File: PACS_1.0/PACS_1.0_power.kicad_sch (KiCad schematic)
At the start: 16 parts, among them U2 TPS562201DDCR, U6 S-1011A70-M6T1U4

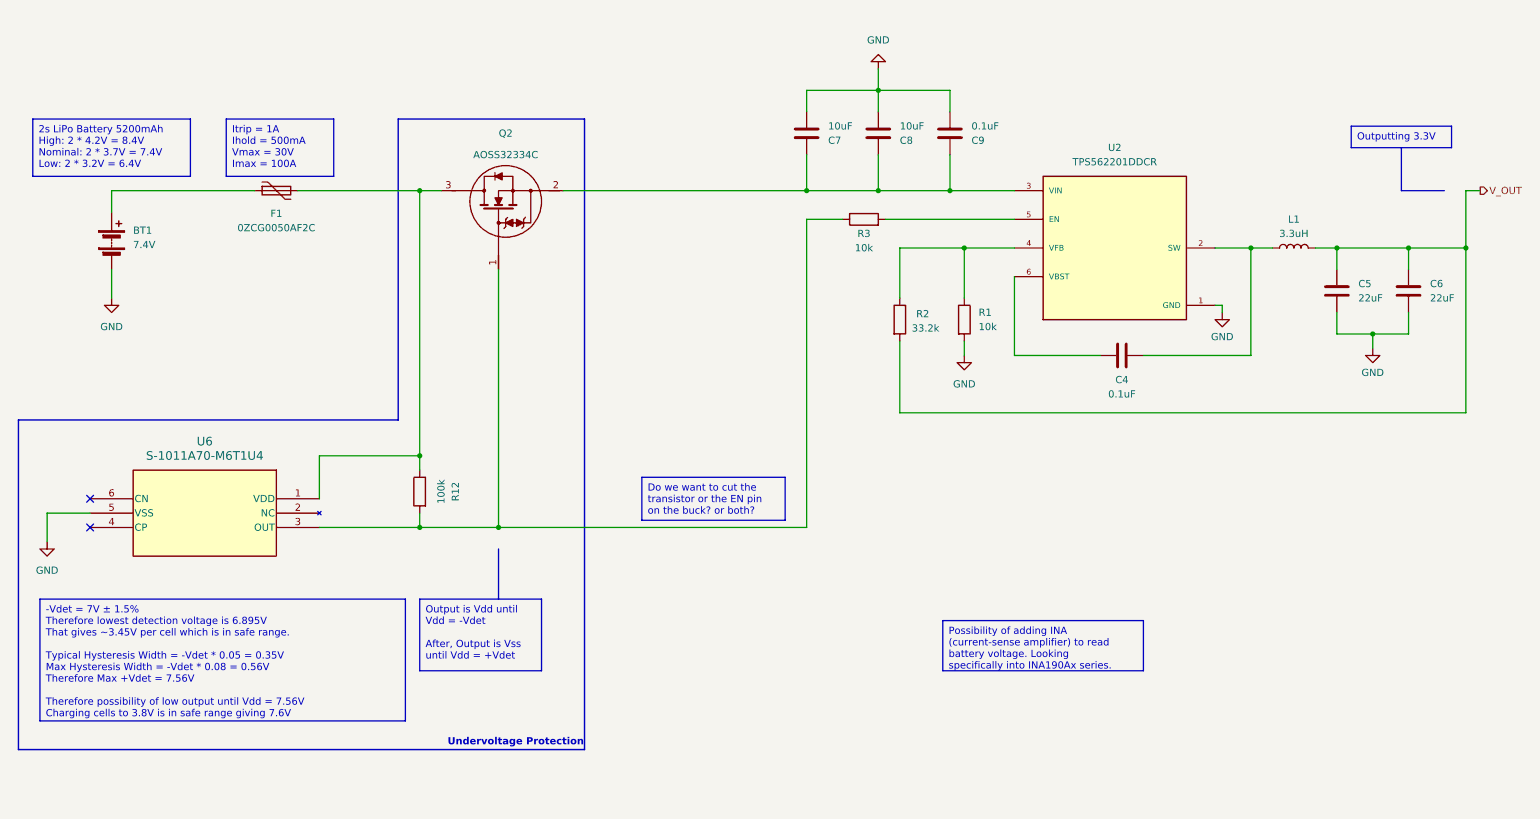
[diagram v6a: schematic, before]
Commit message: Changed Battery
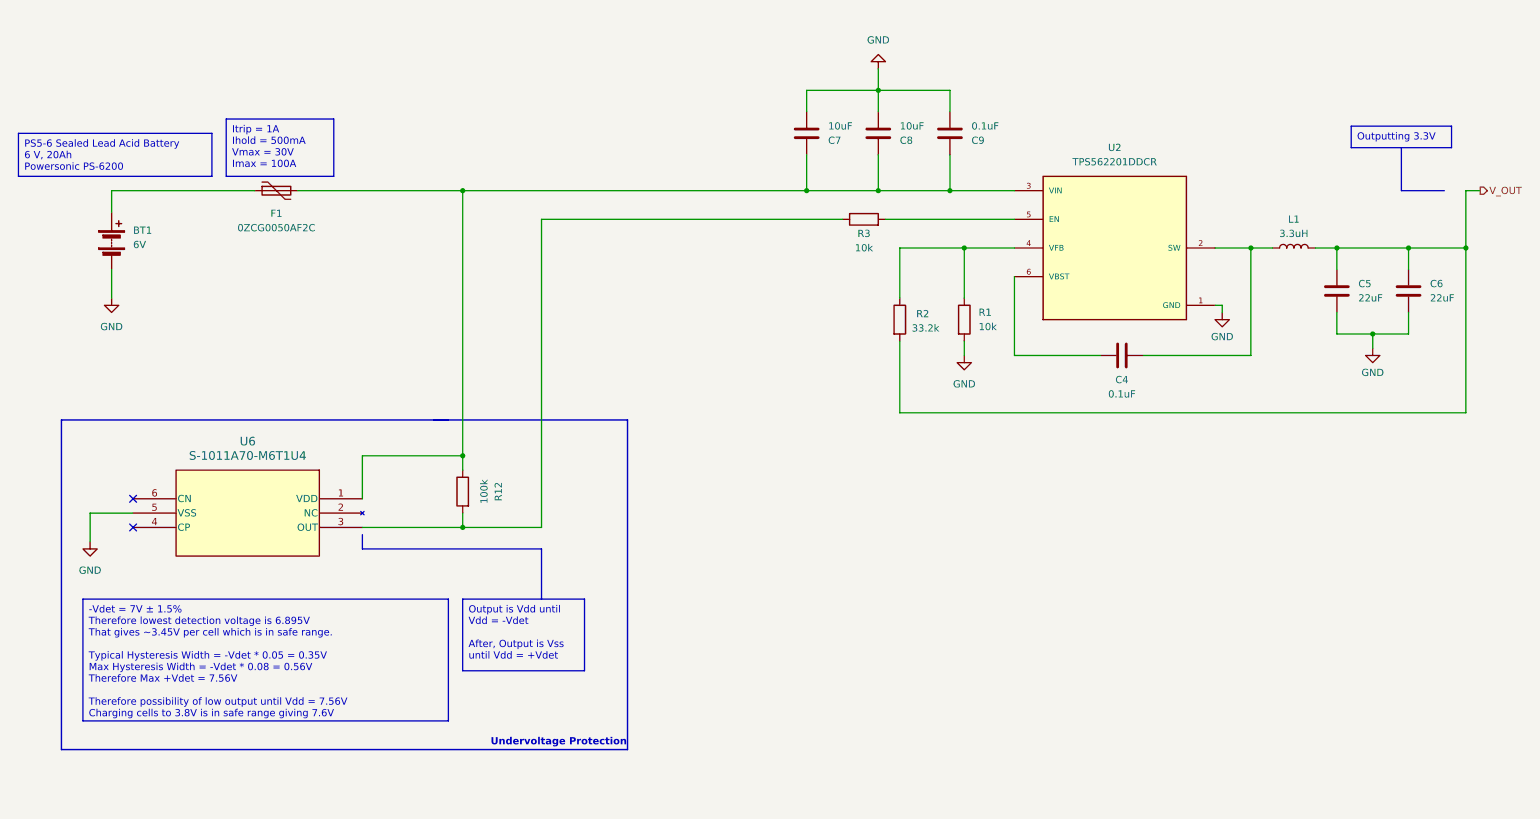
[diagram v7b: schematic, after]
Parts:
- removed Q2: ~, Package_TO_SOT_SMD:TSOT-23, symbol AOSS32334C:AOSS32334C
- BT1: value 7.4V -> 6V
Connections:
- net at C7.1, C8.1, C9.1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: now also F1.2, R12.1, U6.1 (VDD)
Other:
- moved on the sheet: R12, U6

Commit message: Added skeleton for Voltage Divide
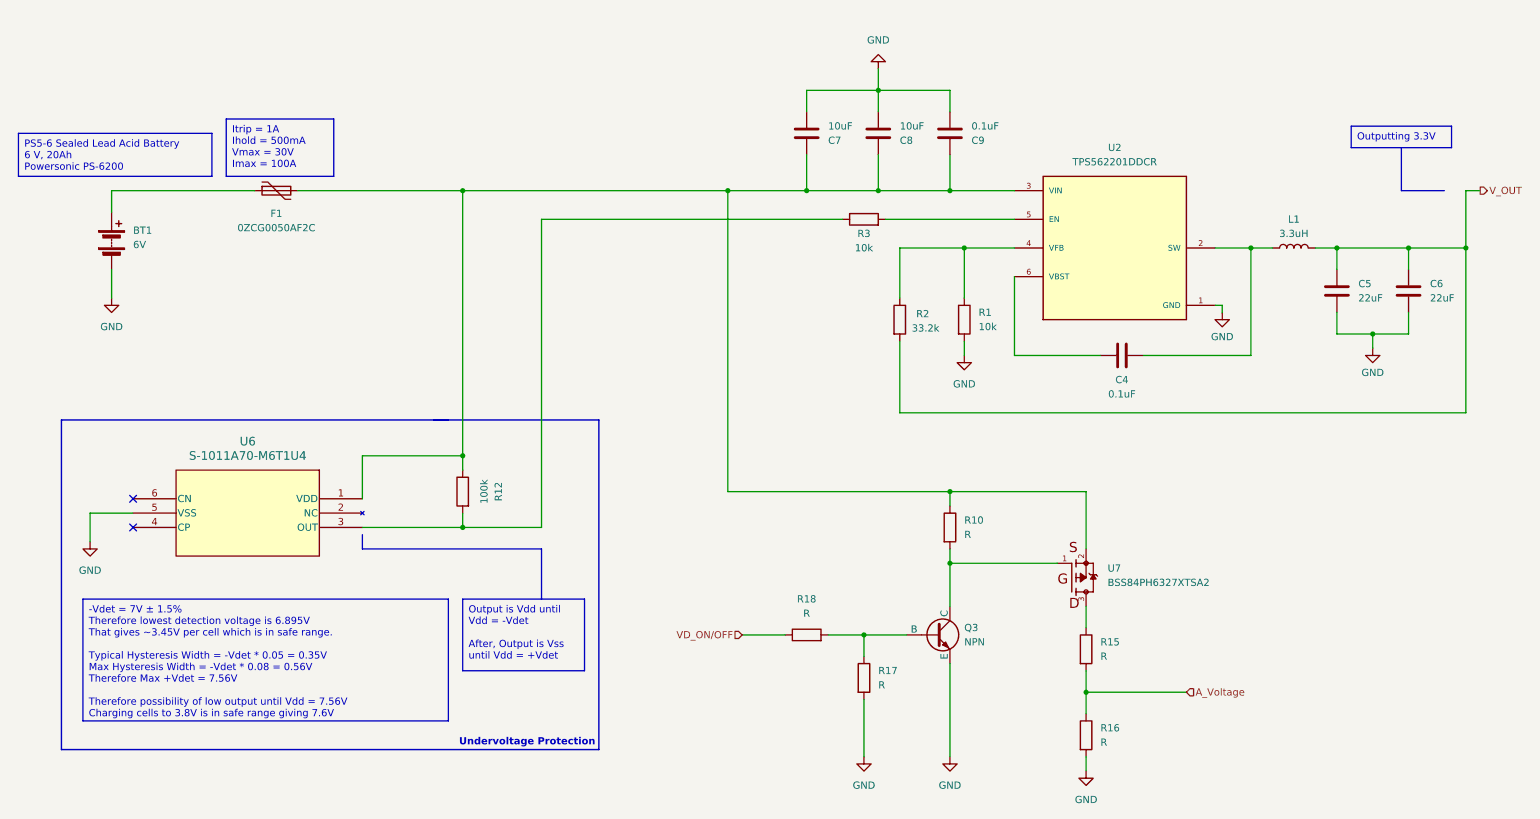
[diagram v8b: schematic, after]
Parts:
- added Q3: NPN, symbol Simulation_SPICE:NPN
- added R10, R15, R16, R17, R18: R, symbol Device:R
- added U7: BSS84PH6327XTSA2, BSS84PH6327XTSA2:SOT-23-3, symbol BSS84PH6327XTSA2:BSS84PH6327XTSA2
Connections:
- net GND: now also Q3.3 (E), R16.2, R17.2
- net at C7.1, C8.1, C9.1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: now also R10.1, U7.2
- new net: Q3.2 (B), R17.1, R18.2
- new net: Q3.1 (C), R10.2, U7.1
- new net: R15.1, U7.3
- new net A_Voltage: R15.2, R16.1
- new net VD_ON/OFF: R18.1
